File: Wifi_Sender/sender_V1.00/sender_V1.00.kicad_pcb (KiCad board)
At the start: 2 copper layers, 96.3 x 80.5 mm, 25 parts, among them J1 Charger, J10 Door_Open, J11 Door_Closed, J12 5V IN, J13 I2C_3, J2 Charge Out, J3 Perimeter, J4 I2C_1, J5 Motor_2, J6 Motor_1, J7 I2C_2, J8 Light Sensor, J9 Green_Red_Led, SW1 PowerSwitch, U1 INA226-Sense_I2C, U2 ESP32-DEVKIT-V1, U3 INA226-Sense_I2C

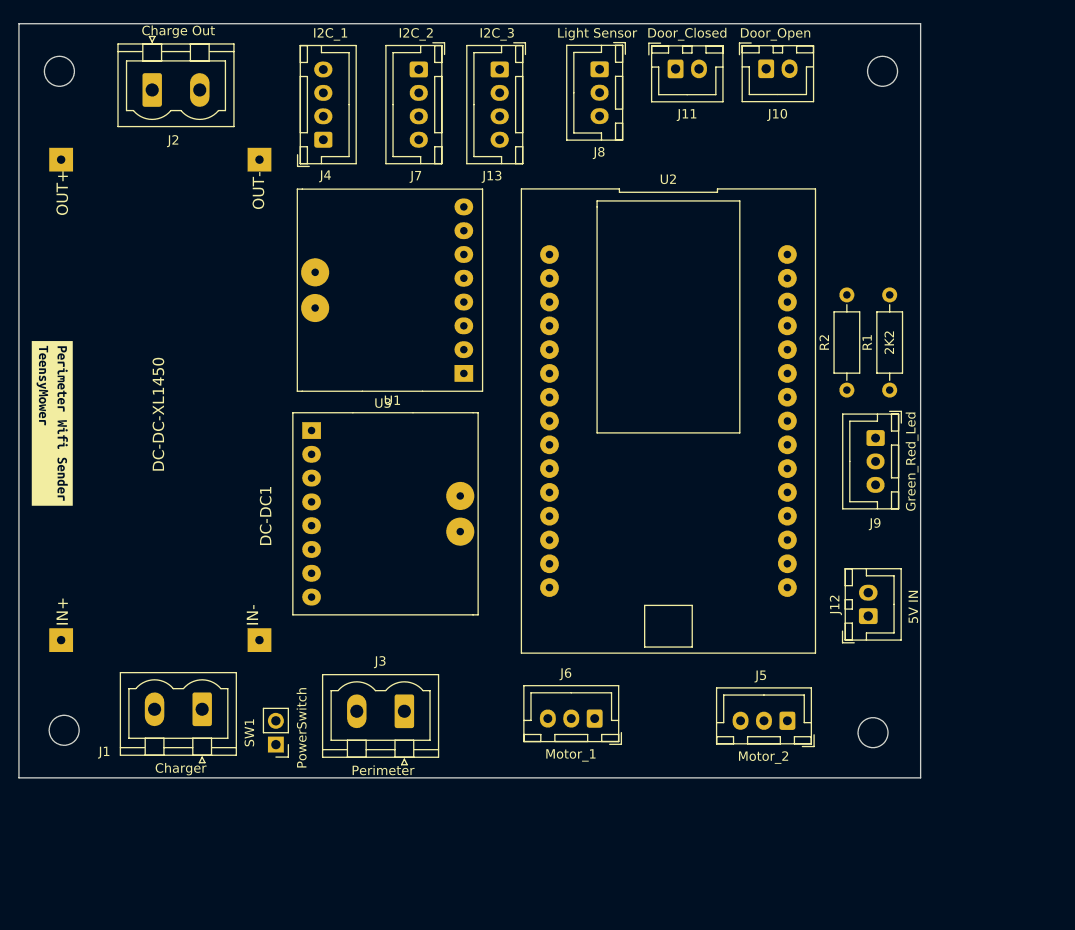
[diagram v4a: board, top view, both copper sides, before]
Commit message: Add Tracks
Tracks added
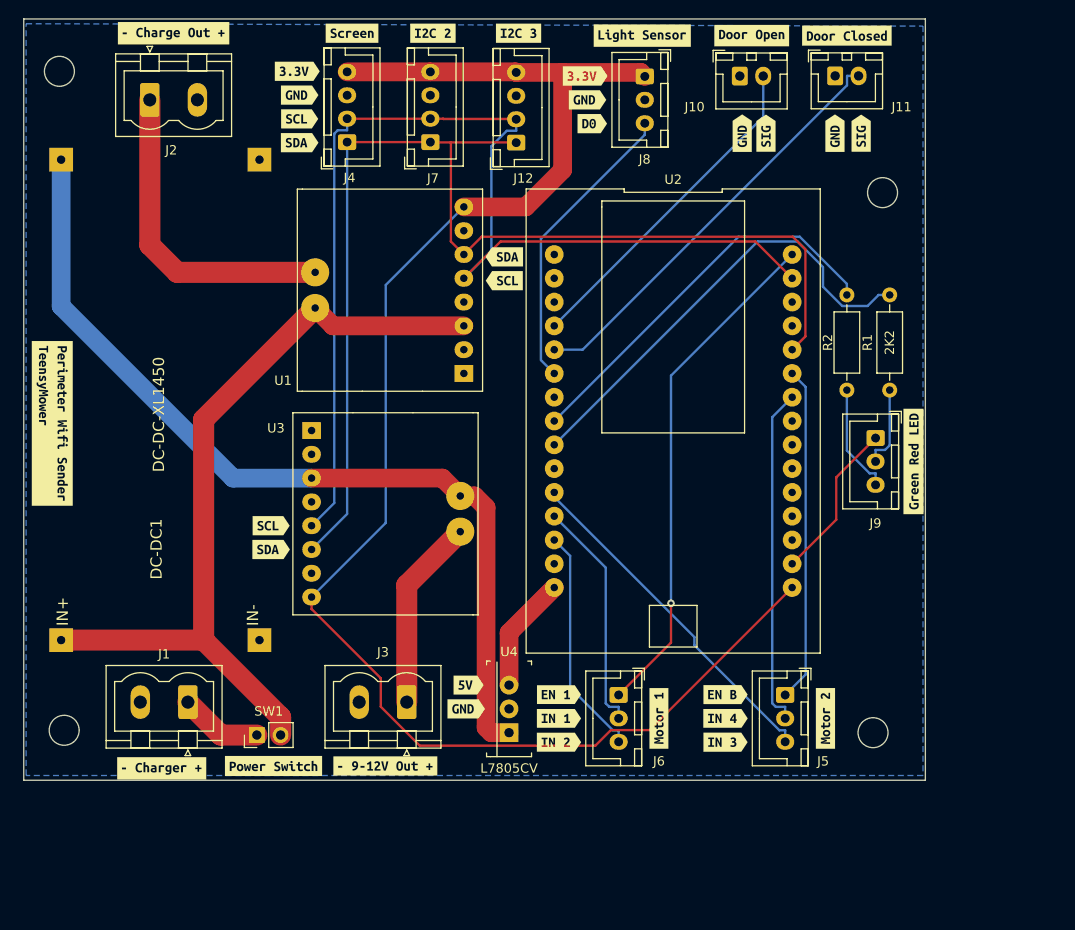
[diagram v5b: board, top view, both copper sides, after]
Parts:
- removed J13: I2C_3, Connector_JST:JST_XH_B4B-XH-A_1x04_P2.50mm_Vertical
- added U4: L7805CV, digikey-footprints:TO-220-3, F.Cu at (86.1, 88.4)
- added kibuzzard-6384DEE7: G***, kibuzzard-6384DEE7, F.Cu at (49.0, 92.2)
- added kibuzzard-6384DF75: G***, kibuzzard-6384DF75, F.Cu at (61.0, 91.9)
- added kibuzzard-6384DFD2: G***, kibuzzard-6384DFD2, F.Cu at (72.9, 91.9)
- added kibuzzard-6384E007: G***, kibuzzard-6384E007, F.Cu at (102.1, 86.9)
- added kibuzzard-6384E151: G***, kibuzzard-6384E151, F.Cu at (91.4, 84.3)
- added kibuzzard-6384E173: G***, kibuzzard-6384E173, F.Cu at (91.4, 86.9)
- added kibuzzard-6384E189: G***, kibuzzard-6384E189, F.Cu at (91.4, 89.4)
- added kibuzzard-6384E1E3: G***, kibuzzard-6384E1E3, F.Cu at (109.2, 89.4)
- added kibuzzard-6384E1F1: G***, kibuzzard-6384E1F1, F.Cu at (109.2, 86.9)
- added kibuzzard-6384E214: G***, kibuzzard-6384E214, F.Cu at (109.2, 84.3)
- added kibuzzard-6384E22C: G***, kibuzzard-6384E22C, F.Cu at (119.9, 86.9)
- added kibuzzard-6384E602: G***, kibuzzard-6384E602, F.Cu at (50.3, 13.7)
- added kibuzzard-6384E652: G***, kibuzzard-6384E652, F.Cu at (69.3, 13.7)
- added kibuzzard-6384E6A4: G***, kibuzzard-6384E6A4, F.Cu at (78.0, 13.7)
- added kibuzzard-6384E6B7: G***, kibuzzard-6384E6B7, F.Cu at (87.1, 13.7)
- added kibuzzard-6384E6DA: G***, kibuzzard-6384E6DA, F.Cu at (63.5, 17.8)
- added kibuzzard-6384E6E7: G***, kibuzzard-6384E6E7, F.Cu at (63.8, 20.3)
- added kibuzzard-6384E6FA: G***, kibuzzard-6384E6FA, F.Cu at (63.8, 22.9)
- added kibuzzard-6384E711: G***, kibuzzard-6384E711, F.Cu at (63.8, 25.4)
- added kibuzzard-6384E779: G***, kibuzzard-6384E779, F.Cu at (100.3, 14.0)
- added kibuzzard-6384E78E: G***, kibuzzard-6384E78E, F.Cu at (94.2, 18.3)
- added kibuzzard-6384E79B: G***, kibuzzard-6384E79B, F.Cu at (94.5, 20.8)
- added kibuzzard-6384E7AB: G***, kibuzzard-6384E7AB, F.Cu at (95.0, 23.4)
- added kibuzzard-6384E7D3: G***, kibuzzard-6384E7D3, F.Cu at (112.0, 14.0)
- added kibuzzard-6384E7EC: G***, kibuzzard-6384E7EC, F.Cu at (111.0, 24.4)
- added kibuzzard-6384E802: G***, kibuzzard-6384E802, F.Cu at (113.5, 24.4)
- added kibuzzard-6384E847: G***, kibuzzard-6384E847, F.Cu at (122.2, 14.0)
- added kibuzzard-6384E870: G***, kibuzzard-6384E870, F.Cu at (120.9, 24.4)
- added kibuzzard-6384E880: G***, kibuzzard-6384E880, F.Cu at (123.7, 24.4)
- added kibuzzard-6384E8E9: G***, kibuzzard-6384E8E9, F.Cu at (129.3, 59.4)
- added kibuzzard-6384E924: G***, kibuzzard-6384E924, F.Cu at (85.6, 37.6)
- added kibuzzard-6384E93F: G***, kibuzzard-6384E93F, F.Cu at (85.6, 40.1)
- added kibuzzard-6384E95B: G***, kibuzzard-6384E95B, F.Cu at (60.7, 66.3)
- added kibuzzard-6384E969: G***, kibuzzard-6384E969, F.Cu at (60.7, 68.8)
- added kibuzzard-63A206E8: G***, kibuzzard-63A206E8, F.Cu at (81.5, 85.9)
- added kibuzzard-63A20733: G***, kibuzzard-63A20733, F.Cu at (81.8, 83.3)
- J12: value 5V IN -> I2C_3; footprint Connector_JST:JST_XH_B2B-XH-A_1x02_P2.50mm_Vertical -> Connector_JST:JST_XH_B4B-XH-A_1x04_P2.50mm_Vertical
- J3: value Perimeter -> 9-12V Out
- J4: value I2C_1 -> Screen (I2C)
- moved J12 63.0 mm to (86.9, 25.4)
- moved J11 17.1 mm to (120.9, 18.3)
- moved H3 13.0 mm to (126.0, 30.7)
- moved J7 7.85 mm to (77.7, 25.3), turned to 90 degrees
- moved J8 4.89 mm to (100.6, 18.3)
- moved J6 3.59 mm to (97.8, 84.4), turned to -90 degrees
- moved J10 2.92 mm to (110.7, 18.3)
- moved J5 2.76 mm to (115.6, 84.4), turned to -90 degrees
- moved J4 2.55 mm to (68.8, 25.3)
- moved SW1 2.28 mm to (59.2, 88.6), turned to 90 degrees
- moved J1 1.70 mm to (51.8, 85.1)
- moved J2 1.09 mm to (47.8, 20.8)
- moved J3 1.01 mm to (75.2, 85.1)
- moved U2 0.51 mm to (103.6, 55.1)
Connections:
- J12 pad 1: GND -> SDA
- J12 pad 2: Net-(U2-Pad15) -> SCL
- U2 pad 16: unconnected-(U2-Pad16) -> +3V3
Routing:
- net +3V3: track 0.00 -> 170.4 mm
- net SDA: track 0.00 -> 124.8 mm
- net SCL: track 0.00 -> 121.8 mm
- net Net-(DC-DC1-PadO+): track 0.00 -> 96.1 mm
- net Net-(DC-DC1-PadI+): track 0.00 -> 85.8 mm
- net Enable_A: track 0.00 -> 54.7 mm, vias 0 -> 1
- net RED: track 0.00 -> 49.4 mm
- net Door_Closed: track 0.00 -> 45.2 mm
- net Green: track 0.00 -> 42.7 mm
- net Input_3: track 0.00 -> 37.2 mm
- net Input_4: track 0.00 -> 36.3 mm
- net Door_Open: track 0.00 -> 35.9 mm
- net Enable_B: track 0.00 -> 35.8 mm
- net Net-(J2-Pad1): track 0.00 -> 34.4 mm
- net D0: track 0.00 -> 31.9 mm
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- added copper zone on B.Cu, net GND
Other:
- board size 96.3 x 80.5 mm -> 96.3 x 81.3 mm
